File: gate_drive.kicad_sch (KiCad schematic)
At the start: 110 parts, among them J19 Conn_01x03, J20 Conn_01x03, U1 EG2131, U14 CC6920B, U2 EG2131, U20 CC6920B, U22 CC6920B, U3 CC6920B, U4 EG2131, U5 EG2131, U7 EG2131, U8 EG2131

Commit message: WORK IN PROGRESS updates from design review - clean schematic and PCB
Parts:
- removed D10, D17, D18, D19, D20, D27, D28, D29, D30, D7, D8, D9: SB10200, parts:TO-277_SB10200, symbol motor_parts:D_Schottky_AKA
- C12, C13, C16, C17, C8, C9: footprint Capacitor_SMD:C_2220_5650Metric -> parts:C_2220_5650Metric_expanded_paste
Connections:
- net A1 renamed M2A_SENSE
- net A2 renamed M2C_SENSE
- net A3 renamed M1A_SENSE
- net A4 renamed M1C_SENSE
- net GPIO10 renamed M2C_PWM_H
- net GPIO11 renamed M2C_PWM_L\
- net GPIO12 renamed M2B_PWM_H
- net GPIO13 renamed M2B_PWM_L\
- net GPIO14 renamed M2A_PWM_H
- net GPIO15 renamed M2A_PWM_L\
- net GPIO4 renamed M1C_PWM_H
- net GPIO5 renamed M1C_PWM_L\
- net GPIO6 renamed M1B_PWM_H
- net GPIO7 renamed M1B_PWM_L\
- net GPIO8 renamed M1A_PWM_H
- net GPIO9 renamed M1A_PWM_L\
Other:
- note added: "MOTOR 1"
- note added: "MOTOR 2"
- note added: "TODO BEFORE PRODUCTION: Add pulldowns to mosfet gates!"
- moved on the sheet: AH1, AH2, AL1, AL2, BH1, BH2, BL1, BL2, C1, C10, C11, C12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

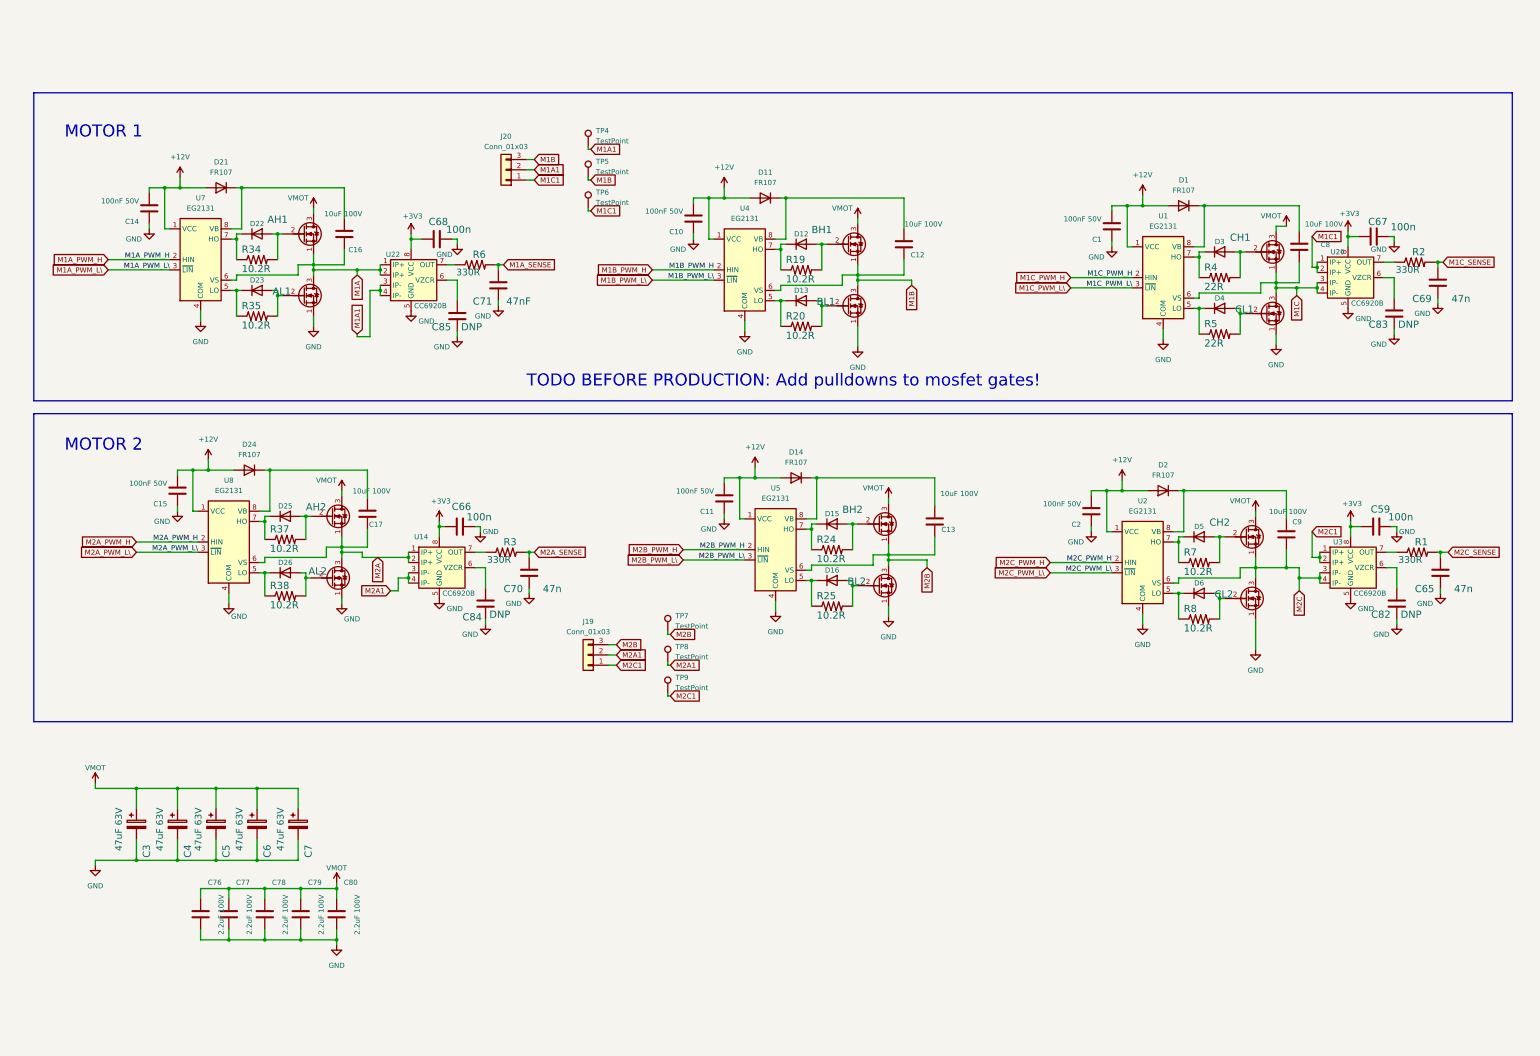
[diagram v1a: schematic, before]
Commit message: Updated schematic based on many suggestions in design review. Incomplete.
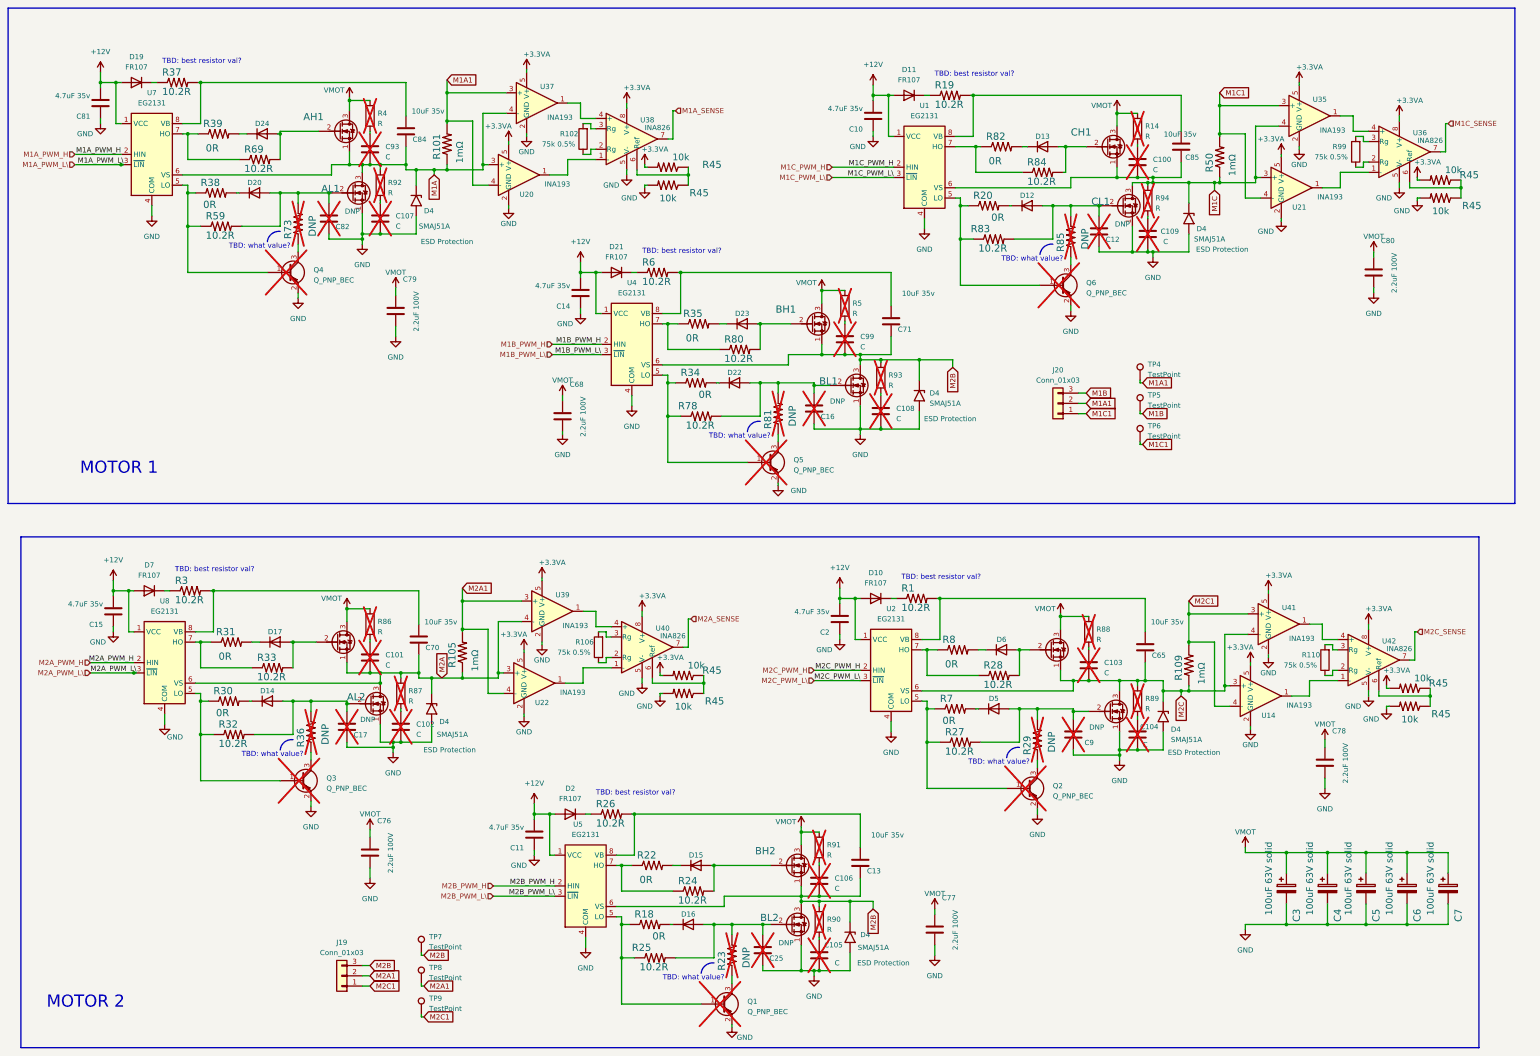
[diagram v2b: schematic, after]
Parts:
- removed C1: 100nF 50V, Capacitor_SMD:C_0603_1608Metric, symbol Device:C
- removed C59, C66, C67: 100n, Capacitor_SMD:C_0603_1608Metric, symbol Device:C
- removed C69: 47n, Capacitor_SMD:C_0603_1608Metric, symbol Device:C
- removed C8: 10uF 100V, parts:C_2220_5650Metric_expanded_paste, symbol Device:C
- removed C83: DNP, Capacitor_SMD:C_0402_1005Metric, symbol Device:C
- removed D1: FR107, Diode_SMD:D_SOD-123, symbol Device:D
- removed D25, D26, D3, D4: 1N4148WS, Diode_SMD:D_SOD-323, symbol Device:D
- removed R2: 330R, Resistor_SMD:R_0603_1608Metric, symbol MotorController:TAYLOR_RESISTOR
- removed R4, R5: 22R, Resistor_SMD:R_0603_1608Metric, symbol MotorController:TAYLOR_RESISTOR
- removed U14, U20, U22, U3: CC6920B, Package_SO:SOIC-8_3.9x4.9mm_P1.27mm, symbol motor_parts:CC6920B
- added C100, C101, C102, C103, C104, C105, C106, C107, C108, C109, C93, C99: C, Capacitor_SMD:C_0603_1608Metric, symbol Device:C
- added C25: DNP, Capacitor_SMD:C_0603_1608Metric, symbol Device:C
- added C81: 4.7uF 35v, Capacitor_SMD:C_0603_1608Metric, symbol Device:C
- added D10, D19, D7: FR107, Diode_SMD:D_SOD-123, symbol Device:D
- added D17, D20: CDBU0130R-HF, Diode_SMD:D_SOD-523, symbol Device:D
- added D4 (x6): SMAJ51A, Diode_SMD:D_SMA, symbol Diode:SMF54A
- added Q1, Q2, Q3, Q4, Q5, Q6: Q_PNP_BEC, Package_TO_SOT_SMD:SOT-23, symbol Device:Q_PNP_BEC
- added R101, R105, R109, R50: 1mΩ, Resistor_SMD:R_2512_6332Metric, symbol MotorController:TAYLOR_RESISTOR
- added R102, R106, R110, R99: 75k 0.5%, Resistor_SMD:R_0603_1608Metric, symbol Device:R
- added R14, R4, R5, R86, R87, R88, R89, R90, R91, R92, R93, R94: R, Resistor_SMD:R_0603_1608Metric, symbol Device:R
- added R18, R22, R30, R31, R39, R82: 0R, Resistor_SMD:R_0603_1608Metric, symbol MotorController:TAYLOR_RESISTOR
- added R23, R29, R36, R73, R81, R85: DNP, Resistor_SMD:R_0603_1608Metric, symbol MotorController:TAYLOR_RESISTOR
- added R26, R27, R28, R32, R33, R59, R69, R78, R80, R83, R84: 10.2R, Resistor_SMD:R_0603_1608Metric, symbol MotorController:TAYLOR_RESISTOR
- added R45 (x8): 10k, Resistor_SMD:R_0603_1608Metric, symbol MotorController:TAYLOR_RESISTOR
- added U14, U20, U21, U22, U35, U37, U39, U41: INA193, Package_TO_SOT_SMD:SOT-23-5, symbol Amplifier_Current:INA193
- added U36, U38, U40, U42: INA826, Package_SO:SO-8_3.9x4.9mm_P1.27mm, symbol motor_parts:INA826
- C10, C11, C14, C15, C2: value 100nF 50V -> 4.7uF 35v; LCSC C14663 -> C162274
- C12, C16, C17, C9: value 10uF 100V -> DNP; footprint parts:C_2220_5650Metric_expanded_paste -> Capacitor_SMD:C_0603_1608Metric; LCSC C2843466 -> (none); now not fitted; now left out of the parts list
- C13: value 10uF 100V -> 10uF 35v; footprint parts:C_2220_5650Metric_expanded_paste -> Capacitor_SMD:C_0603_1608Metric; LCSC C2843466 -> C194427
- C3, C4, C5, C6, C7: value 47uF 63V -> 100uF 63V solid; footprint Capacitor_SMD:CP_Elec_8x10 -> Capacitor_THT:CP_Radial_D8.0mm_P3.50mm; LCSC C72524 -> C2898915
- C65, C70: value 47n -> 10uF 35v; LCSC C1622 -> C194427
- C68: value 100n -> 2.2uF 100V; footprint Capacitor_SMD:C_0603_1608Metric -> Capacitor_SMD:C_1206_3216Metric; LCSC C14663 -> C650969
- C71: value 47nF -> 10uF 35v; LCSC C1622 -> C194427
- C82: footprint Capacitor_SMD:C_0402_1005Metric -> Capacitor_SMD:C_0603_1608Metric; now not fitted; now left out of the parts list
- C84, C85: value DNP -> 10uF 35v; footprint Capacitor_SMD:C_0402_1005Metric -> Capacitor_SMD:C_0603_1608Metric; LCSC (none) -> C194427
- D12, D13, D15, D16, D22, D23, D5, D6: value 1N4148WS -> CDBU0130R-HF; footprint Diode_SMD:D_SOD-323 -> Diode_SMD:D_SOD-523; LCSC C2128 -> C3012732
- D14, D24: value FR107 -> CDBU0130R-HF; footprint Diode_SMD:D_SOD-123 -> Diode_SMD:D_SOD-523; LCSC C511885 -> C3012732
- R1, R3, R6: value 330R -> 10.2R; LCSC C105881 -> C22773
- R20, R34, R35, R38, R7, R8: value 10.2R -> 0R; LCSC C22773 -> C21189
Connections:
- net +3V3 is gone; now on net VMOT: C68.1
- net +12V: now also C81.2, D10.2 (A), D19.2 (A), D7.2 (A); no longer D14.2 (A), D24.2 (A)
- net GND: now also C12.1, C16.1, C17.1, C9.1, C102.2, C104.2, C105.2, C107.2, C108.2, C109.2, C25.1, C81.1, D4.2 (A2), D4.2 (A2), D4.2 (A2), D4.2 (A2), D4.2 (A2), D4.2 (A2), Q1.2 (E), Q2.2 (E), Q3.2 (E), Q4.2 (E), Q5.2 (E), Q6.2 (E), R45.2, R45.2, R45.2, R45.2, U14.2 (GND), U20.2 (GND), U21.2 (GND), U22.2 (GND), U35.2 (GND), U36.5 (V-), U37.2 (GND), U38.5 (V-), U39.2 (GND), U40.5 (V-), U41.2 (GND), U42.5 (V-); no longer C65.1, C70.1, C71.1, C84.1, C85.1
- net M1A: now also C84.1, C93.2, D4.1 (A1), R101.1, R92.1, U20.3 (+), U37.4 (-); no longer C16.1
- net M1A1: now also R101.2, U20.4 (-), U37.3 (+)
- net M1A_SENSE: now also U38.7; no longer C71.2, R6.2
- net M1B: no longer BH1.1 (S), BL1.3 (D), C12.1, U4.6 (VS)
- net M1C: now also C85.1, C100.2, D4.1 (A1), R50.1, R94.1, U21.3 (+), U35.4 (-)
- net M1C1: now also R50.2, U21.4 (-), U35.3 (+)
- net M1C_SENSE: now also U36.7
- net M2A: now also C70.1, C101.2, D4.1 (A1), R105.1, R87.1, U22.3 (+), U39.4 (-); no longer C17.1
- net M2A1: now also R105.2, U22.4 (-), U39.3 (+)
- net M2A_SENSE: now also U40.7; no longer C70.2, R3.2
- net M2B: now also BH1.1 (S), BL1.3 (D), C71.1, U4.6 (VS), C106.2, C99.2, D4.1 (A1), D4.1 (A1), R90.1, R93.1
- net M2C: now also C65.1, C103.2, D4.1 (A1), R109.1, R89.1, U14.3 (+), U41.4 (-); no longer C9.1
- net M2C1: now also R109.2, U14.4 (-), U41.3 (+)
- net M2C_SENSE: now also U42.7; no longer C65.2, R1.2
- net VMOT: now also R14.1, R4.1, R5.1, R86.1, R88.1, R91.1
- net at R37.1: now also D19.1 (K); no longer U8.7 (HO)
- net at R37.2: now also C84.2, U7.8 (VB); no longer AH2.2 (G)
- net at U1.7 (HO): now also R82.1, R84.1
- net at CH1.2 (G): now also D13.2 (A), R84.2
- net at R24.1, U5.7 (HO): now also R22.1; no longer D15.1 (K)
- net at R38.1: now also U7.5 (LO), Q4.1 (B), R59.1; no longer U8.5 (LO)
- net at BL2.2 (G), D16.2 (A), R25.2: now also C25.2, R23.2
- net at R25.1, U5.5 (LO): now also Q1.1 (B), R18.1; no longer D16.1 (K)
- net at C13.2, U5.8 (VB): now also R26.2; no longer D14.1 (K)
- net at C85.2: now also R19.2, U1.8 (VB)
- net at U1.5 (LO): now also R20.1, Q6.1 (B), R83.1
- net at CL1.2 (G): now also C12.2, D12.2 (A), R83.2, R85.2
- net at R38.2: now also D20.1 (K); no longer AL2.2 (G)
- net at R1.1: now also D10.1 (K)
- net at R3.1: now also D7.1 (K)
- net at R6.1: now also D21.1 (K)
- net at C82.2: now also AL1.2 (G), D20.2 (A), R59.2, R73.2
- new net: R45.1, R45.1, U38.6 (Ref)
- new net: D24.1 (K), R39.2
- new net: AH1.2 (G), D24.2 (A), R69.2
- new net: C100.1, R14.2
- new net: C9.2, CL2.2 (G), D5.2 (A), R27.2, R29.2
- new net: AH2.2 (G), D17.2 (A), R33.2
- new net: C65.2, R1.2, U2.8 (VB)
- new net: C108.1, R93.2
- new net: R45.1, R45.1, U36.6 (Ref)
- new net: R99.1, U36.2 (Rg)
- new net: R99.2, U36.3 (Rg)
- new net: C103.1, R88.2
- new net: C71.2, R6.2, U4.8 (VB)
- new net: R45.1, R45.1, U42.6 (Ref)
- new net: R35.1, R80.1, U4.7 (HO)
- new net: BH1.2 (G), D23.2 (A), R80.2
- new net: Q5.1 (B), R34.1, R78.1, U4.5 (LO)
- new net: D15.1 (K), R22.2
- new net: Q1.3 (C), R23.1
- new net: BL1.2 (G), C16.2, D22.2 (A), R78.2, R81.2
- new net: Q3.1 (B), R30.1, R32.1, U8.5 (LO)
- new net: R31.1, R33.1, U8.7 (HO)
- new net: C70.2, R3.2, U8.8 (VB)
- new net: CH2.2 (G), D6.2 (A), R28.2
- new net: C105.1, R90.2
- new net: C107.1, R92.2
- new net: C99.1, R5.2
- new net: Q2.1 (B), R27.1, R7.1, U2.5 (LO)
- new net: D5.1 (K), R7.2
- new net: Q2.3 (C), R29.1
- new net: R45.1, R45.1, U40.6 (Ref)
- new net: D2.1 (K), R26.1
- new net: U39.1, U40.4 (+)
- new net: C104.1, R89.2
- new net: D22.1 (K), R34.2
- new net: U21.1, U36.1 (-)
- new net: U35.1, U36.4 (+)
- new net: D16.1 (K), R18.2
- new net: R110.1, U42.2 (Rg)
- new net: R110.2, U42.3 (Rg)
- new net: AL2.2 (G), C17.2, D14.2 (A), R32.2, R36.2
- new net: C93.1, R4.2
- new net: C101.1, R86.2
- new net: U22.1, U40.1 (-)
- new net: R106.1, U40.2 (Rg)
- new net: R106.2, U40.3 (Rg)
- new net: D11.1 (K), R19.1
- new net: U37.1, U38.4 (+)
- new net: R39.1, R69.1, U7.7 (HO)
- new net: D14.1 (K), R30.2
- new net: D12.1 (K), R20.2
- new net: Q5.3 (C), R81.1
- new net: Q3.3 (C), R36.1
- new net: D17.1 (K), R31.2
- new net: U41.1, U42.4 (+)
- new net: Q6.3 (C), R85.1
- new net: Q4.3 (C), R73.1
- new net: D6.1 (K), R8.2
- new net: D13.1 (K), R82.2
- new net: R28.1, R8.1, U2.7 (HO)
- new net: D23.1 (K), R35.2
- new net: C109.1, R94.2
- new net: C102.1, R87.2
- new net: C106.1, R91.2
- new net: U14.1, U42.1 (-)
- new net: R102.1, U38.2 (Rg)
- new net: R102.2, U38.3 (Rg)
- new net: U20.1, U38.1 (-)
- new net +3.3VA: R45.2, R45.2, R45.2, R45.2, U14.5 (V+), U20.5 (V+), U21.5 (V+), U22.5 (V+), U35.5 (V+), U36.8 (V+), U37.5 (V+), U38.8 (V+), U39.5 (V+), U40.8 (V+), U41.5 (V+), U42.8 (V+)
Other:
- note added: "TBD: best resistor val?"
- note added: "TBD: what value?"
- note removed: "TODO BEFORE PRODUCTION: Add pulldowns to mosfet gates!"
- moved on the sheet: AH1, AL1, AL2, BH1, BH2, BL1, BL2, C11, C13, C3, C4, C5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

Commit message: Replaced global labels with normal net labels
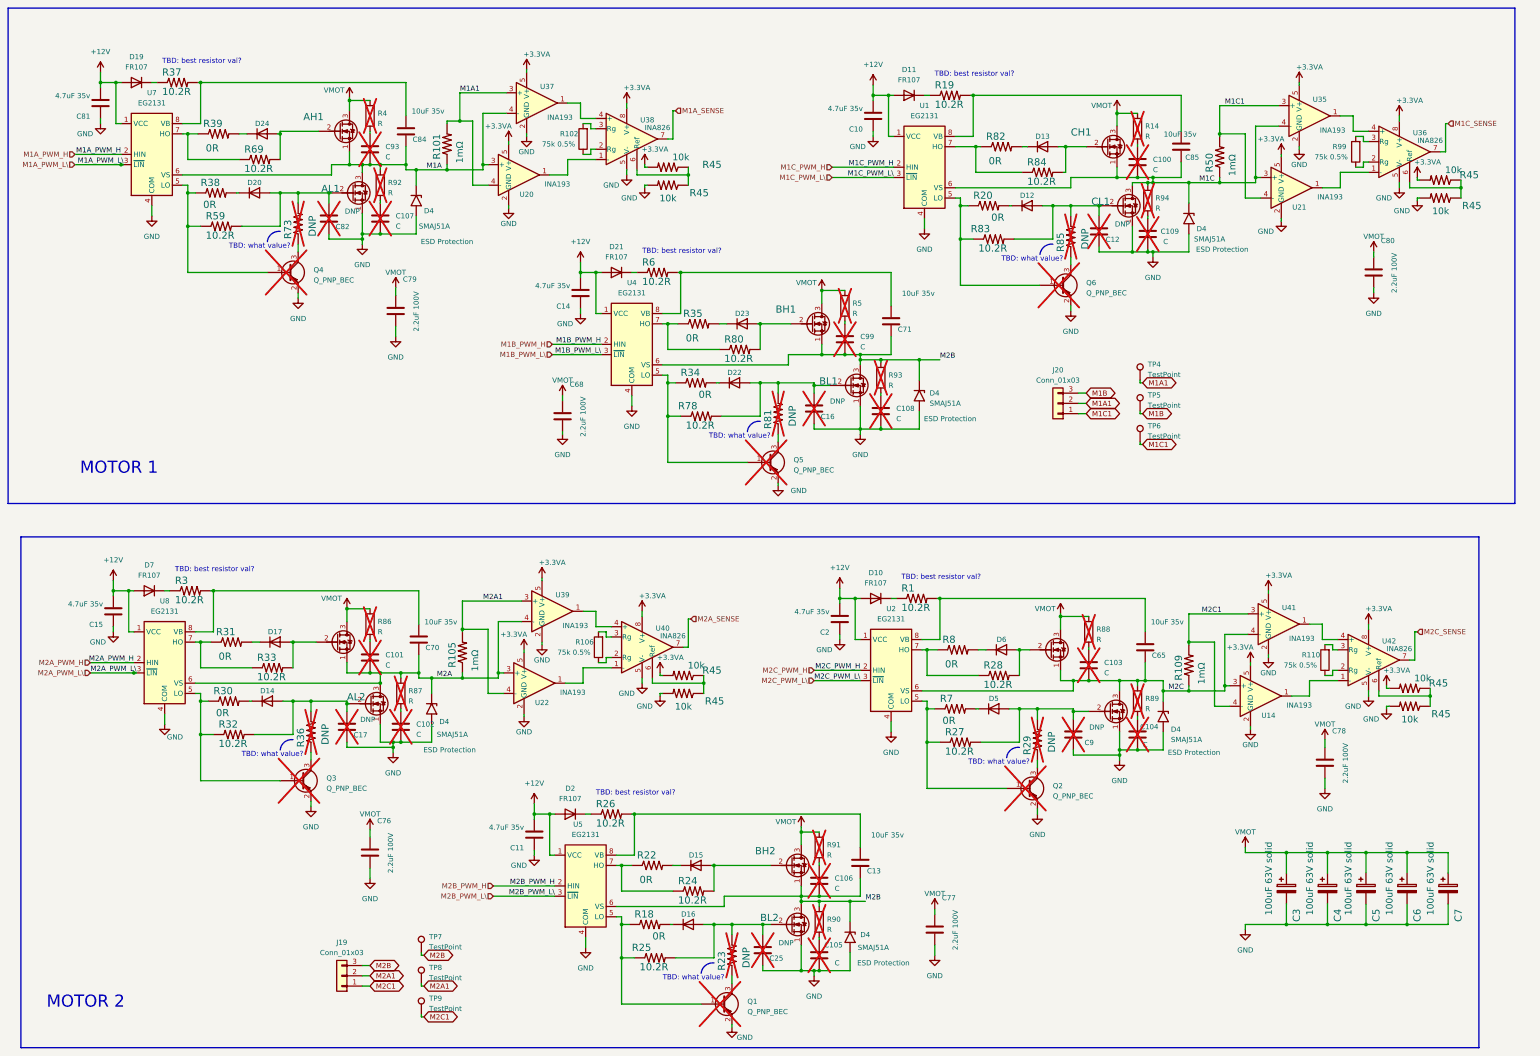
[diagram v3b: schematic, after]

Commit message: Work in progress, starting to place components.
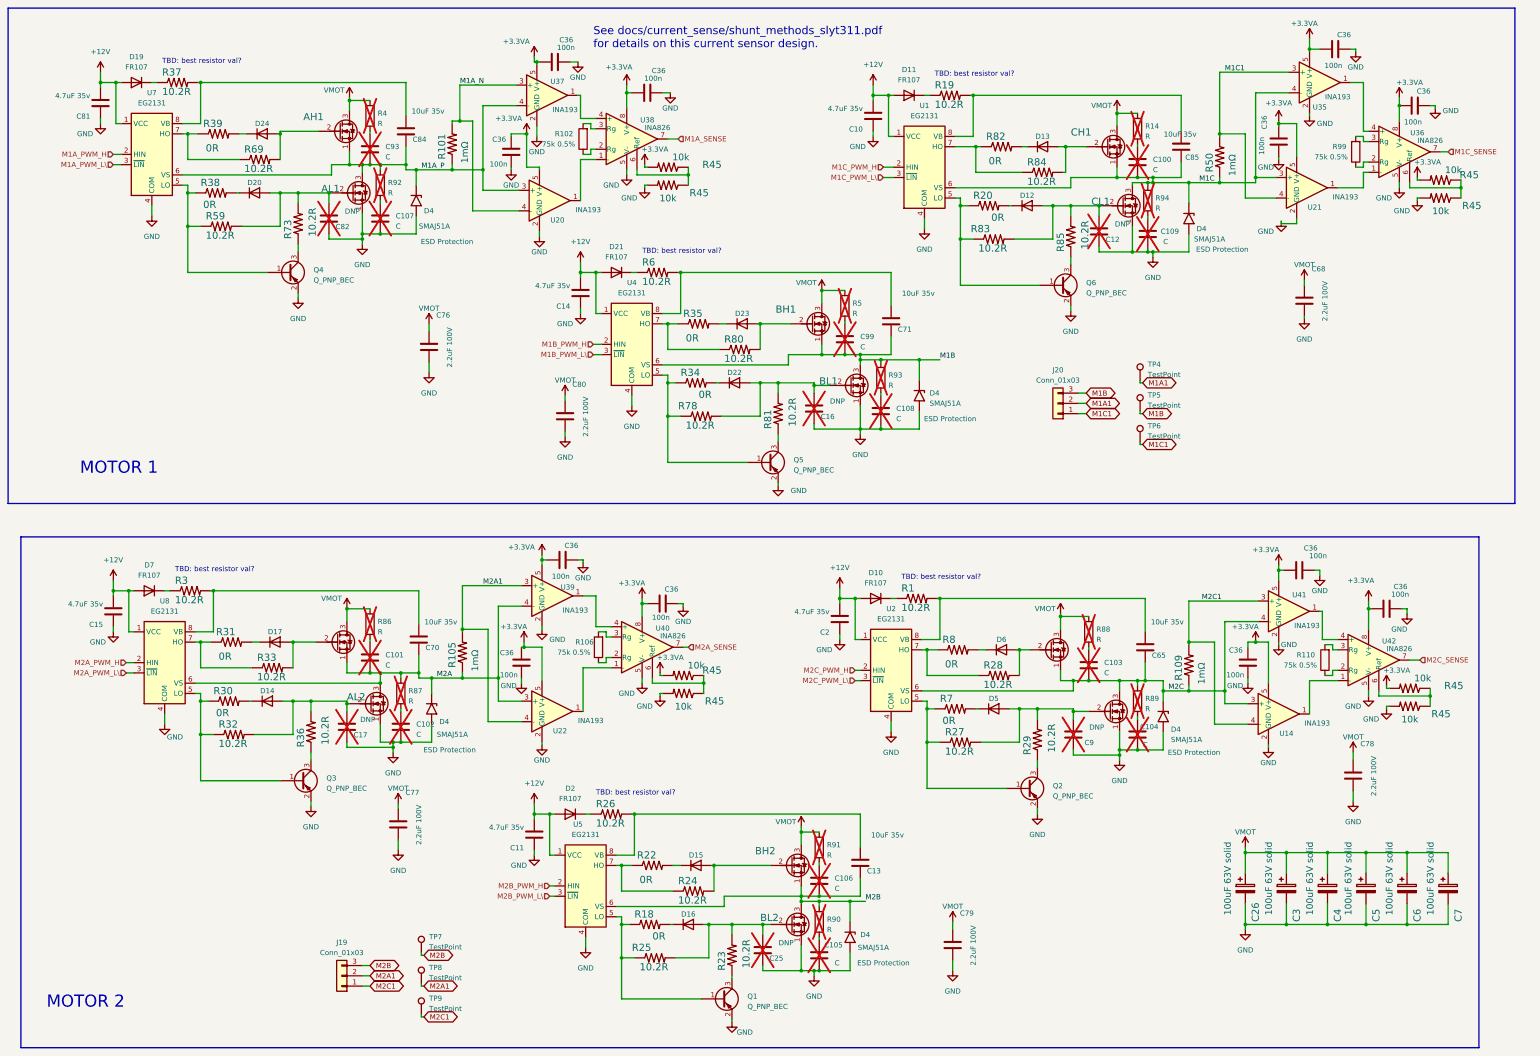
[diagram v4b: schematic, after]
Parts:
- added C26: 100uF 63V solid, Capacitor_THT:CP_Radial_D8.0mm_P3.50mm, symbol Device:C_Polarized
- added C36 (x12): 100n, Capacitor_SMD:C_0603_1608Metric, symbol Device:C
- Q1, Q2, Q3, Q4, Q5, Q6: now fitted; now in the parts list
- R23, R29, R36, R73, R81, R85: value DNP -> 10.2R; LCSC (none) -> C22773; now fitted
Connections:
- net +3.3VA: now also C36.1, C36.1, C36.1, C36.1, C36.1, C36.1, C36.1, C36.1, C36.1, C36.1, C36.1, C36.2
- net GND: now also C26.2, C36.1, C36.2, C36.2, C36.2, C36.2, C36.2, C36.2, C36.2, C36.2, C36.2, C36.2, C36.2
- net M1A1: no longer R101.2, U20.4 (-), U37.3 (+)
- net M1B: now also BH1.1 (S), BL1.3 (D), C71.1, C99.2, D4.1 (A1), R93.1, U4.6 (VS)
- net M2B: no longer BH1.1 (S), BL1.3 (D), C71.1, C99.2, D4.1 (A1), R93.1, U4.6 (VS)
- net VMOT: now also C26.1
- net M1A renamed M1A_P
- new net M1A_N: R101.2, U20.4 (-), U37.3 (+)
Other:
- note added: "See docs/current_sense/shunt_methods_slyt311.pdf for details on this current sensor design."
- note removed: "TBD: what value?"
- moved on the sheet: C68, C76, C77, C78, C79, C80, R101, U14, U20, U21, U22, U35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
